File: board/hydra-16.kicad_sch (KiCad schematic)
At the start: 32 parts, among them J1 Conn_01x32, J2 Conn_01x24, J3 DE9_Plug, U3 AT28C64B, U4 W65C02SxP, U5 6522, U6 6551, U7 MAX232, U8 628512_DIP32, U9 74LS154

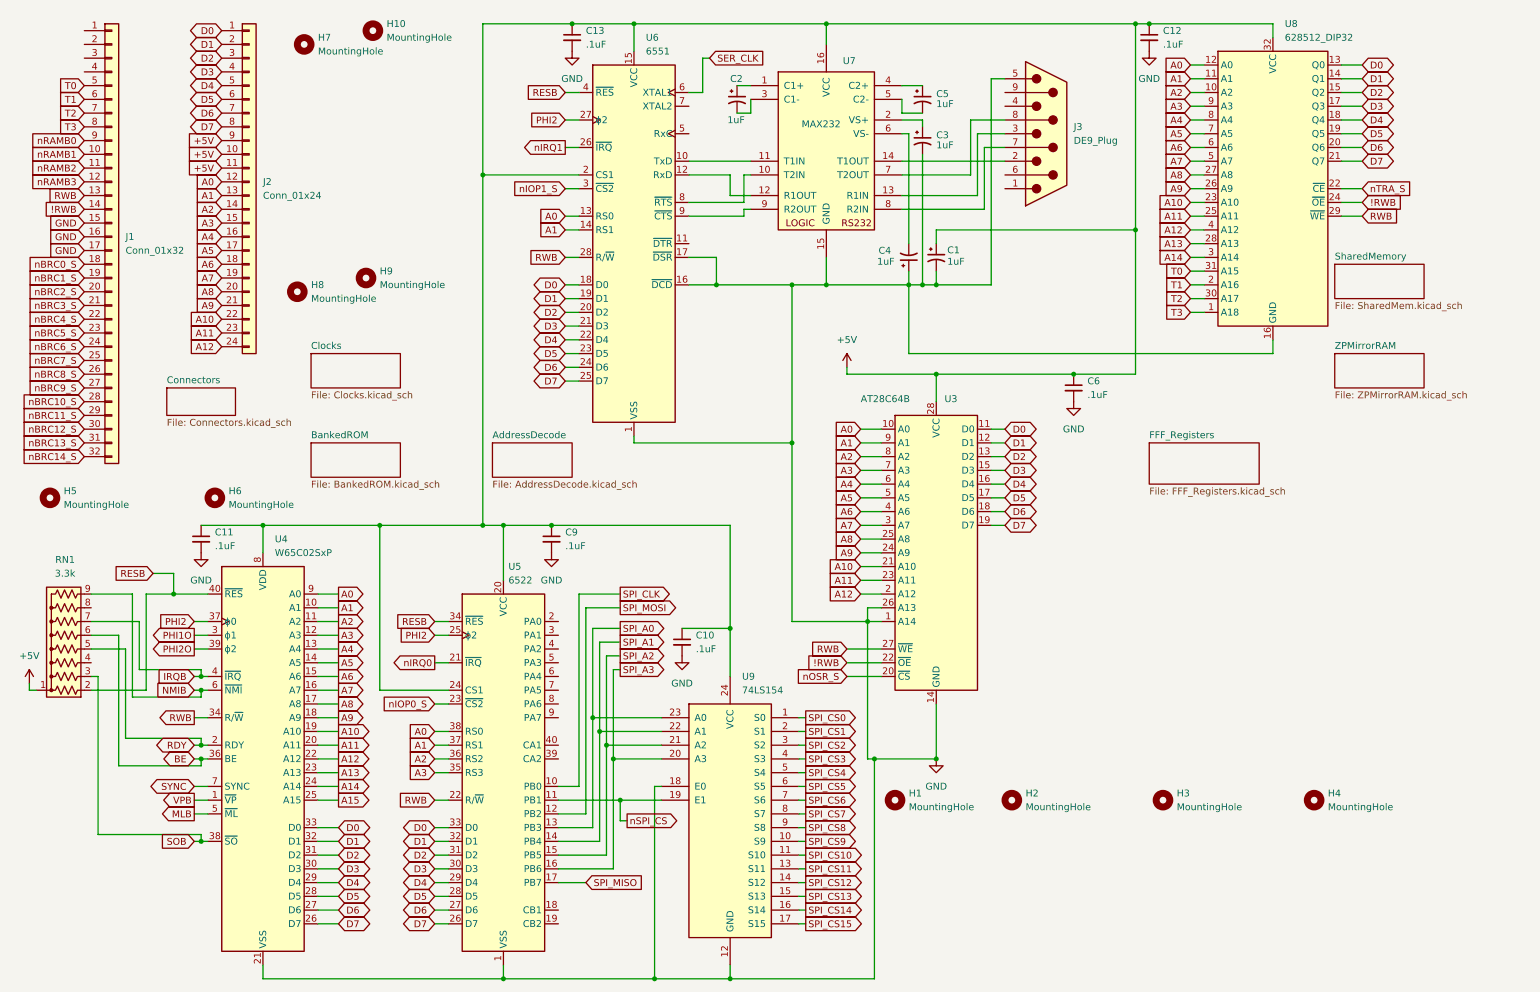
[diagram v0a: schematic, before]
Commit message: Updated schematics with larger mounting holes (4mm vs 3.2mm) and larger electrolytic cap footprints
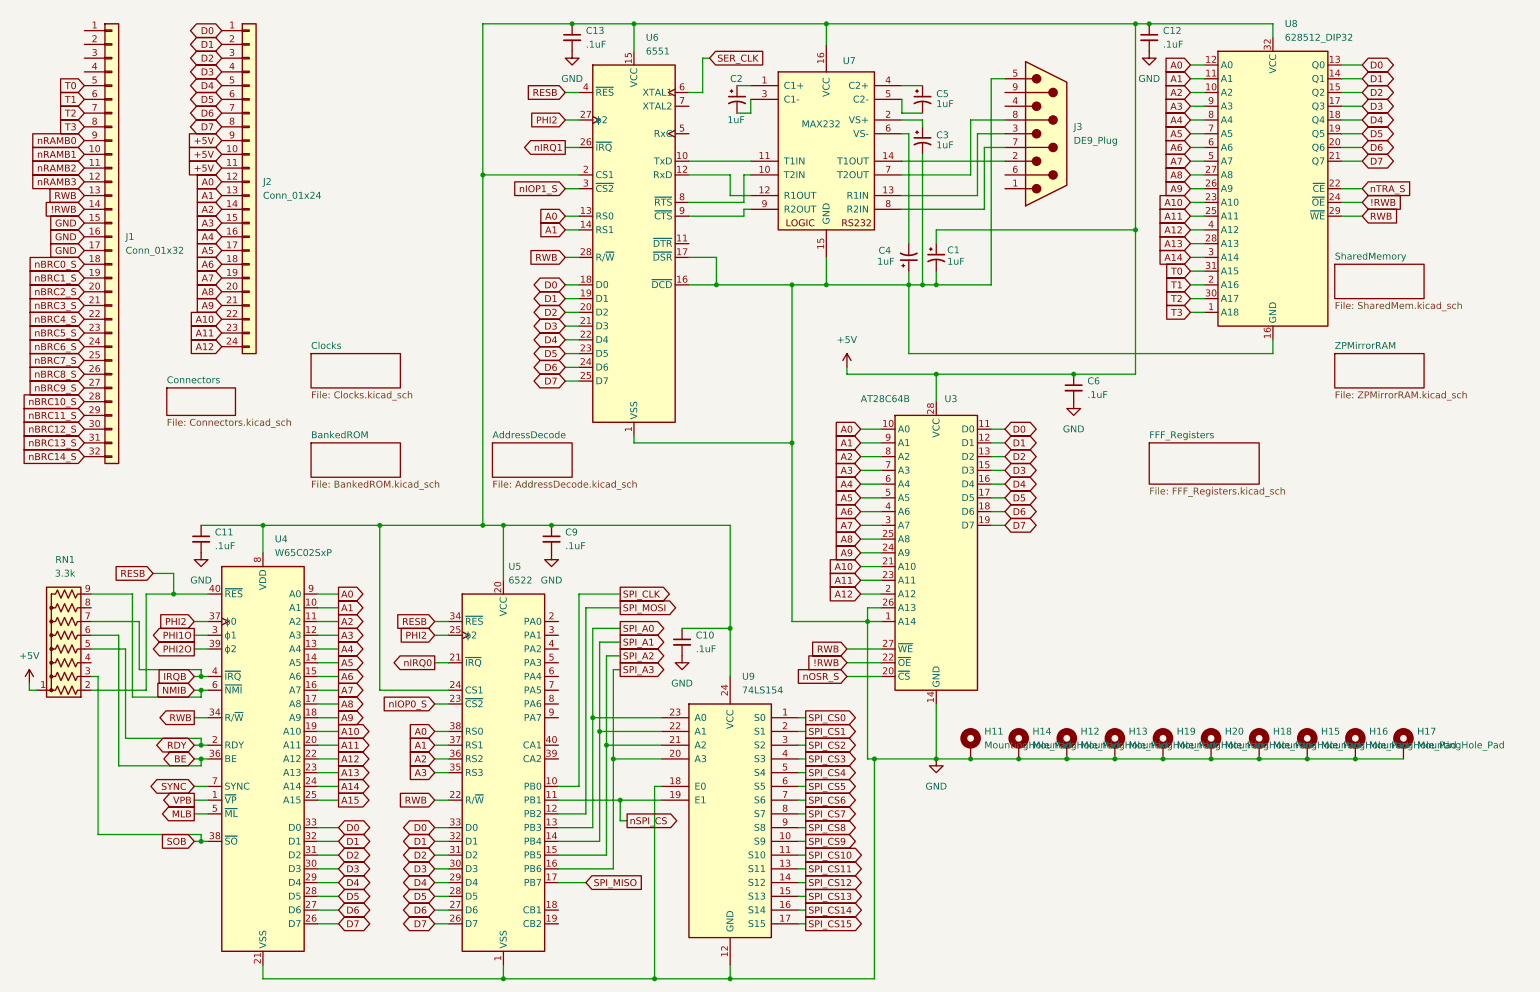
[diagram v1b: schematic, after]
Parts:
- removed H1, H10, H2, H3, H4, H5, H6, H7, H8, H9: MountingHole, MountingHole:MountingHole_3.2mm_M3_Pad_TopBottom, symbol Mechanical:MountingHole
- added H11, H12, H13, H14, H15, H16, H17, H18, H19, H20: MountingHole_Pad, MountingHole:MountingHole_4mm_Pad_TopBottom, symbol Mechanical:MountingHole_Pad
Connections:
- net GND: now also H11.1, H12.1, H13.1, H14.1, H15.1, H16.1, H17.1, H18.1, H19.1, H20.1

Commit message: Schematic Bus updates, silkscreen updates, position tweaks, and other corrections.
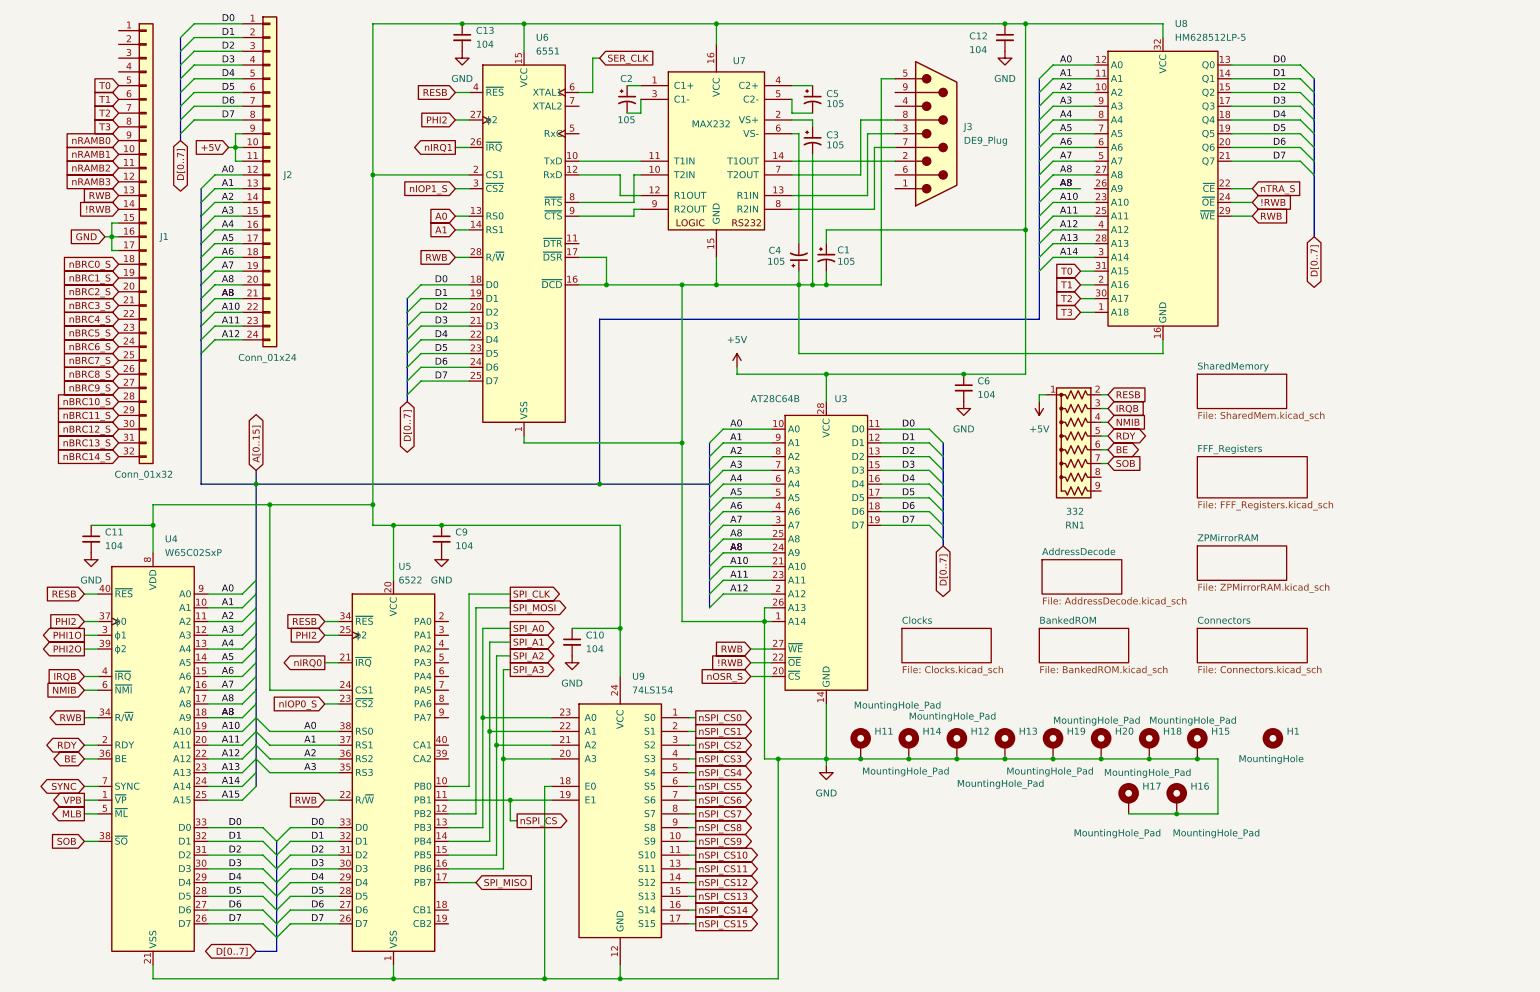
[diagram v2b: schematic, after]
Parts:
- added H1: MountingHole, MountingHole:MountingHole_4mm, symbol Mechanical:MountingHole
- C1, C2, C3, C4, C5: value 1uF -> 105
- C10, C11, C12, C13, C6, C9: value .1uF -> 104
- RN1: value 3.3k -> 332
- U8: value 628512_DIP32 -> HM628512LP-5
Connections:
- net A8: now also J2.21 (Pin_21), U3.24 (A9), U4.18 (A9)
- net IRQB: now also RN1.3 (R2); no longer RN1.7 (R6)
- net NMIB: now also RN1.4 (R3); no longer RN1.9 (R8)
- net SOB: now also RN1.7 (R6); no longer RN1.3 (R2)
- removed net A9: J2.21 (Pin_21), U3.24 (A9), U4.18 (A9), U8.26 (A9)
- net SPI_CS0 renamed nSPI_CS0
- net SPI_CS1 renamed nSPI_CS1
- net SPI_CS10 renamed nSPI_CS10
- net SPI_CS11 renamed nSPI_CS11
- net SPI_CS12 renamed nSPI_CS12
- net SPI_CS13 renamed nSPI_CS13
- net SPI_CS14 renamed nSPI_CS14
- net SPI_CS15 renamed nSPI_CS15
- net SPI_CS2 renamed nSPI_CS2
- net SPI_CS3 renamed nSPI_CS3
- net SPI_CS4 renamed nSPI_CS4
- net SPI_CS5 renamed nSPI_CS5
- net SPI_CS6 renamed nSPI_CS6
- net SPI_CS7 renamed nSPI_CS7
- net SPI_CS8 renamed nSPI_CS8
- net SPI_CS9 renamed nSPI_CS9
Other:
- company: (none) -> Data Tuning
- title: (none) -> CPU, VIA, ACIA, O/S ROM, Task RAM and Banked RAM Connector
- moved on the sheet: C1, C10, C11, C12, C13, C2, C3, C4, C5, C6, C9, H11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

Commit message: More PCB position tweaks.
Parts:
- U4: value W65C02SxP -> W65C02S
- U5: value 6522 -> 65C22
- U6: value 6551 -> 65C51
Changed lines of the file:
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@@
 			)
 		)
-		(property "Value" "6522"
+		(property "Value" "65C22"
 			(at 84.7441 119.38 0)
 			(effects
@@
 			)
 		)
-		(property "Value" "6551"
+		(property "Value" "65C51"
 			(at 110.1441 21.59 0)
 			(effects
@@
 			)
 		)
-		(property "Value" "W65C02SxP"
+		(property "Value" "W65C02S"
 			(at 41.5641 114.3 0)
 			(effects

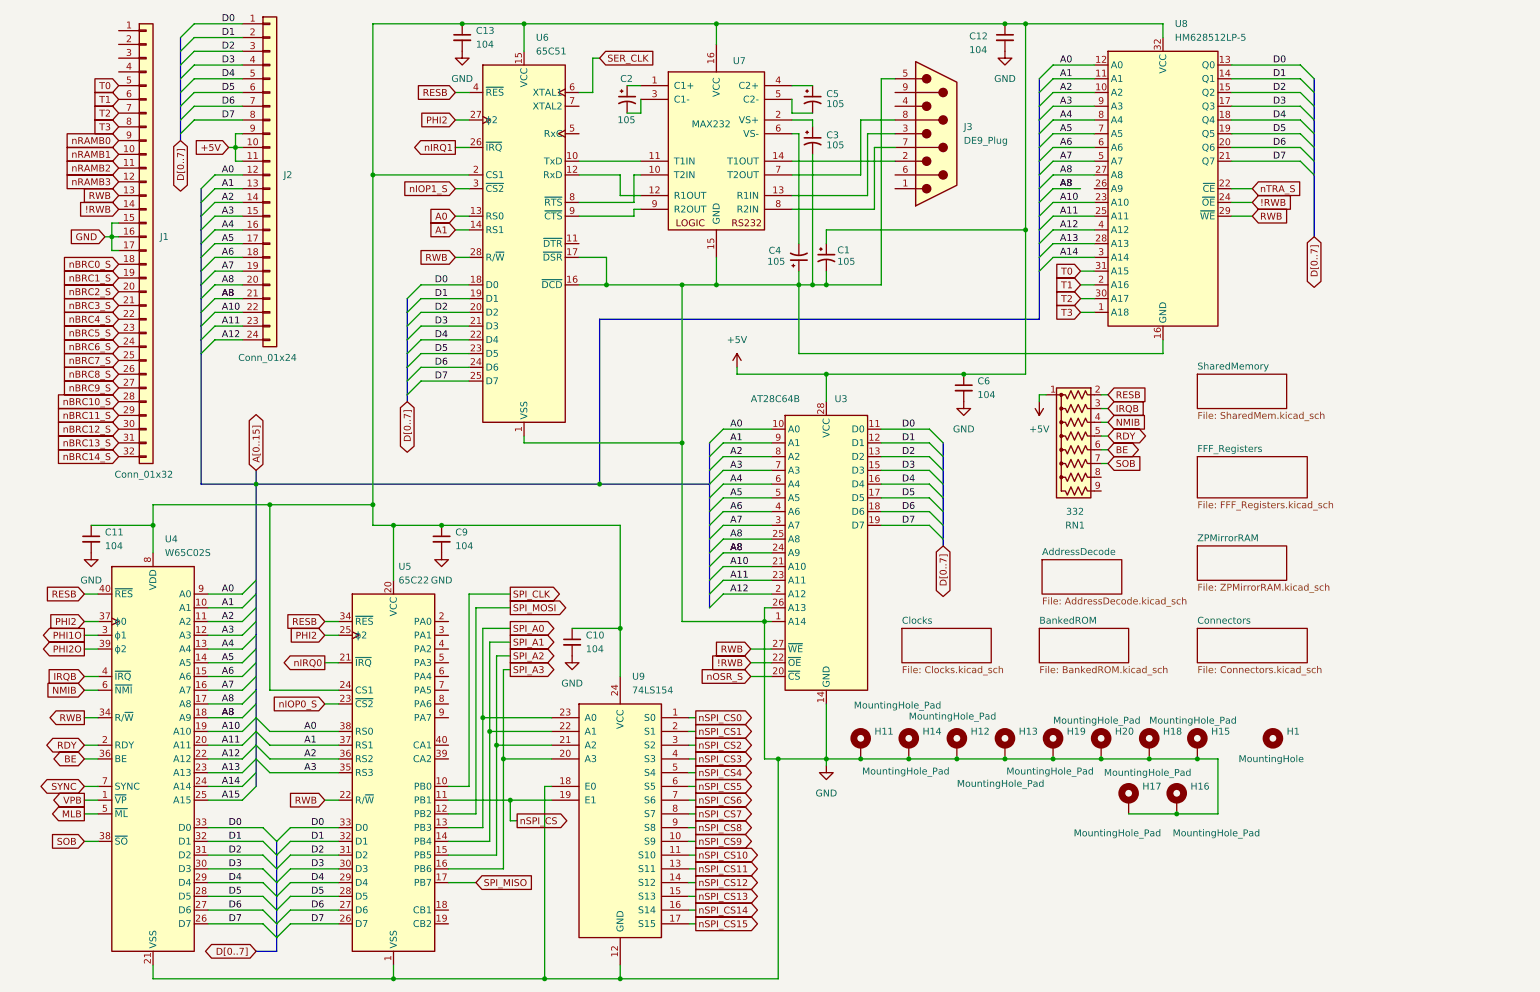
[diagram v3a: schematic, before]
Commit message: Latest PCB and schematic updates.  Moved some stuff around to help flow and added some labels.
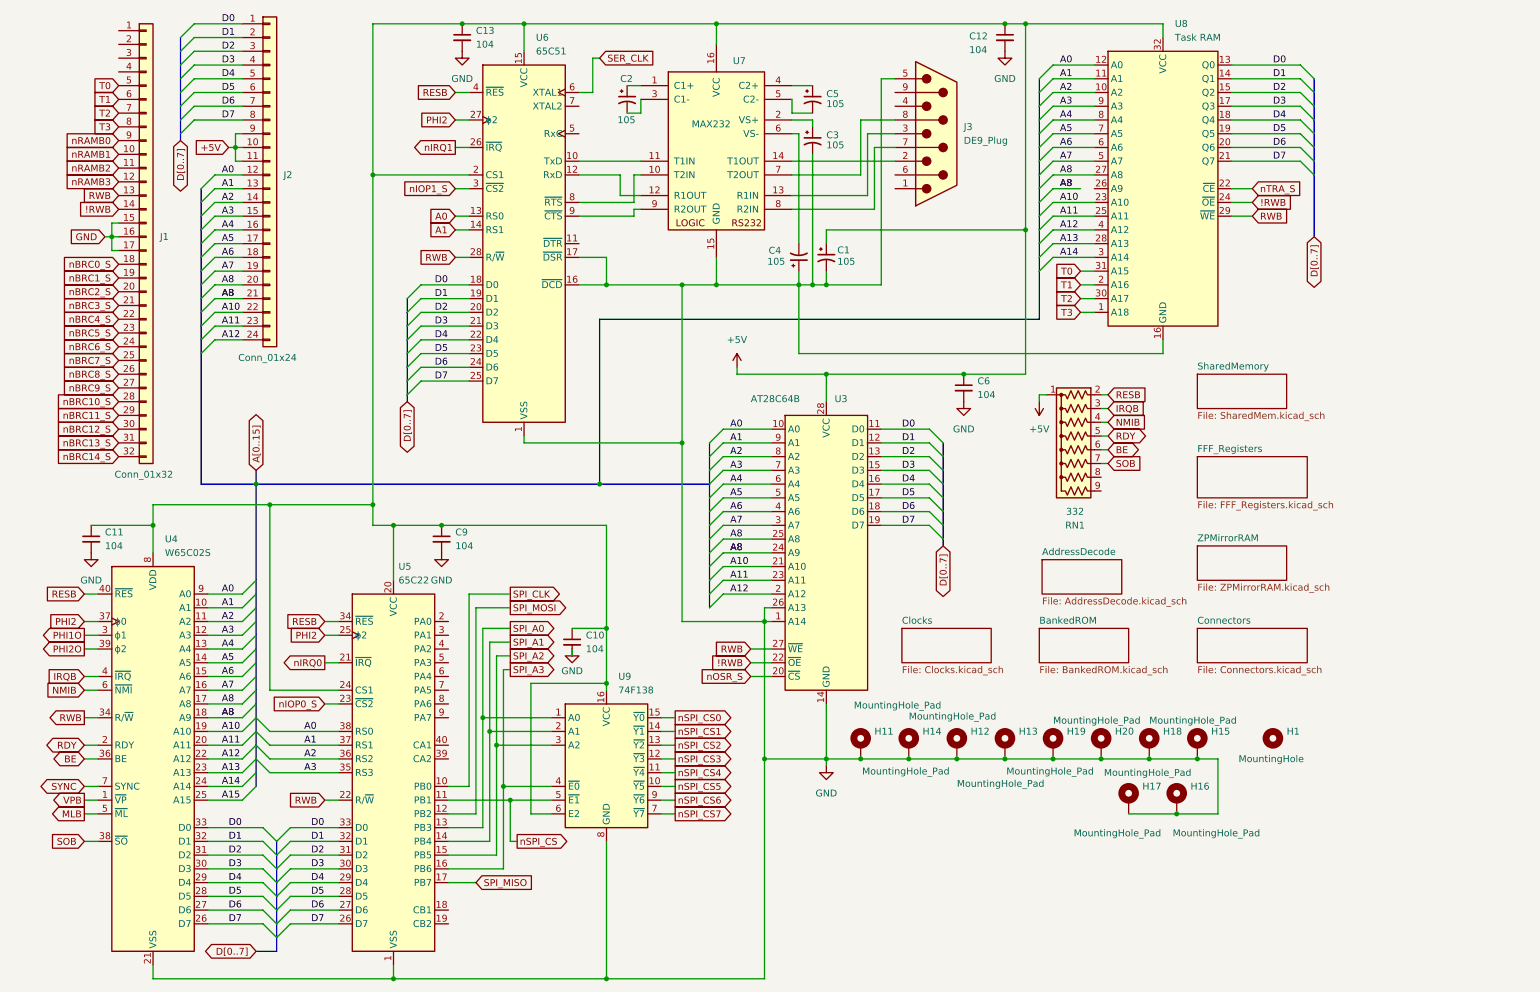
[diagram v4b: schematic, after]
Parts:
- removed U9: 74LS154, Package_DIP:DIP-24_W15.24mm_Socket_LongPads, symbol 74xx:74LS154
- added U9: 74F138, Package_DIP:DIP-16_W7.62mm_Socket_LongPads, symbol 74xx:74HC138
- U8: value HM628512LP-5 -> Task RAM
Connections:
- net +5V: now also U9.16 (VCC), U9.6 (E2)
- net GND: now also U9.8 (GND)
- net SPI_A0: now also U9.1 (A0)
- net SPI_A1: now also U9.2 (A1)
- net SPI_A2: now also U9.3 (A2)
- net SPI_A3: now also U9.4 (~{E0})
- net nSPI_CS: now also U9.5 (~{E1})
- net nSPI_CS0: now also U9.15 (~{Y0})
- net nSPI_CS1: now also U9.14 (~{Y1})
- net nSPI_CS2: now also U9.13 (~{Y2})
- net nSPI_CS3: now also U9.12 (~{Y3})
- net nSPI_CS4: now also U9.11 (~{Y4})
- net nSPI_CS5: now also U9.10 (~{Y5})
- net nSPI_CS6: now also U9.9 (~{Y6})
- net nSPI_CS7: now also U9.7 (~{Y7})

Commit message: Moving external resources into source.
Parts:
- J1: footprint Connector_PinHeader_2.54mm:PinHeader_1x32_P2.54mm_Vertical -> Connector_PinSocket_2.54mm:PinSocket_1x32_P2.54mm_Vertical
- J2: footprint Connector_PinHeader_2.54mm:PinHeader_1x24_P2.54mm_Vertical -> Connector_PinSocket_2.54mm:PinSocket_1x24_P2.54mm_Vertical
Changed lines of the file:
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@@
 			)
 		)
-		(property "Footprint" "Connector_PinHeader_2.54mm:PinHeader_1x24_P2.54mm_Vertical"
+		(property "Footprint" "Connector_PinSocket_2.54mm:PinSocket_1x24_P2.54mm_Vertical"
 			(at 60.96 44.45 0)
 			(effects
@@
 			)
 		)
-		(property "Footprint" "Connector_PinHeader_2.54mm:PinHeader_1x32_P2.54mm_Vertical"
+		(property "Footprint" "Connector_PinSocket_2.54mm:PinSocket_1x32_P2.54mm_Vertical"
 			(at 38.1 55.88 0)
 			(effects

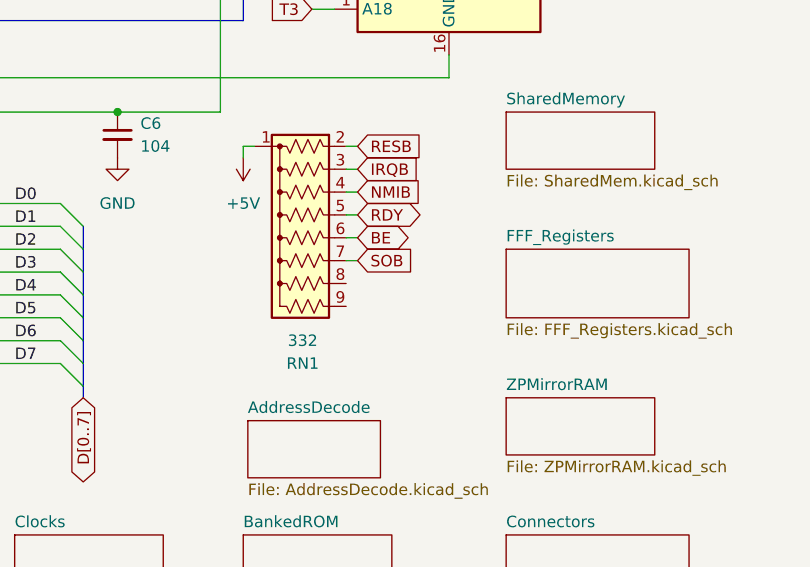
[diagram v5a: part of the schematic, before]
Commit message: Fixing nBROMD routing, removing unnecessary 7404, and minor other cleanup.
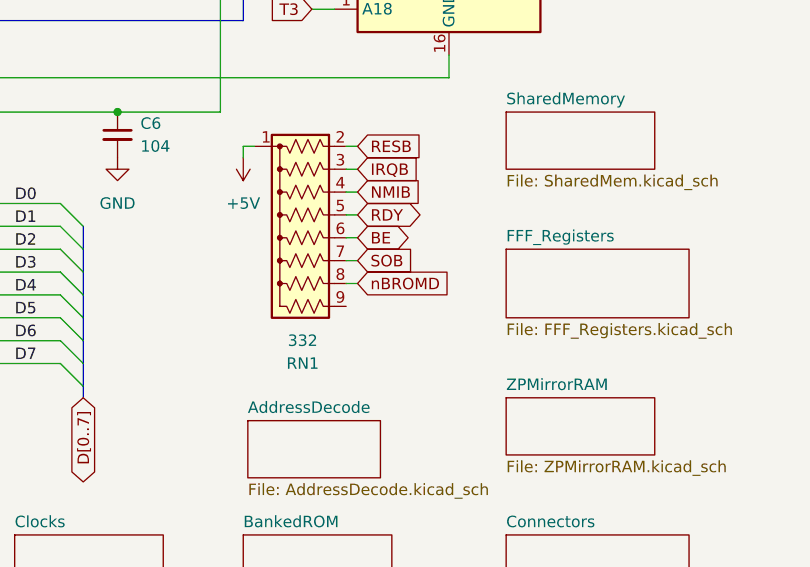
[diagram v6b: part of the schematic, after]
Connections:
- net nBROMD: now reaches RN1.8 (R7)
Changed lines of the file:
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@@
+	(wire
+		(pts
+			(xy 215.9 100.33) (xy 214.63 100.33)
+		)
+		(stroke
+			(width 0)
+			(type default)
+		)
+	)
 	(wire
 		(pts
@@
 			(effects
 				(font
+					(size 1.27 1.27)
+				)
+				(justify left)
+				(hide yes)
+			)
+		)
+	)
+	(global_label "nBROMD"
+		(shape input)
+		(at 215.9 100.33 0)
+		(fields_autoplaced yes)
+		(effects
+			(font
+				(size 1.27 1.27)
+			)
+			(justify left)
+		)
+		(property "Intersheetrefs" "${INTERSHEET_REFS}"
+			(at 226.6261 100.33 0)
+			(effects
+				(font
